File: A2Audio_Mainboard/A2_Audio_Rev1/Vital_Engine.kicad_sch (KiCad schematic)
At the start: 13 parts, among them J4 Micro_SD_Card, J5 Conn_01x15, U26 TS5A3159DBVR

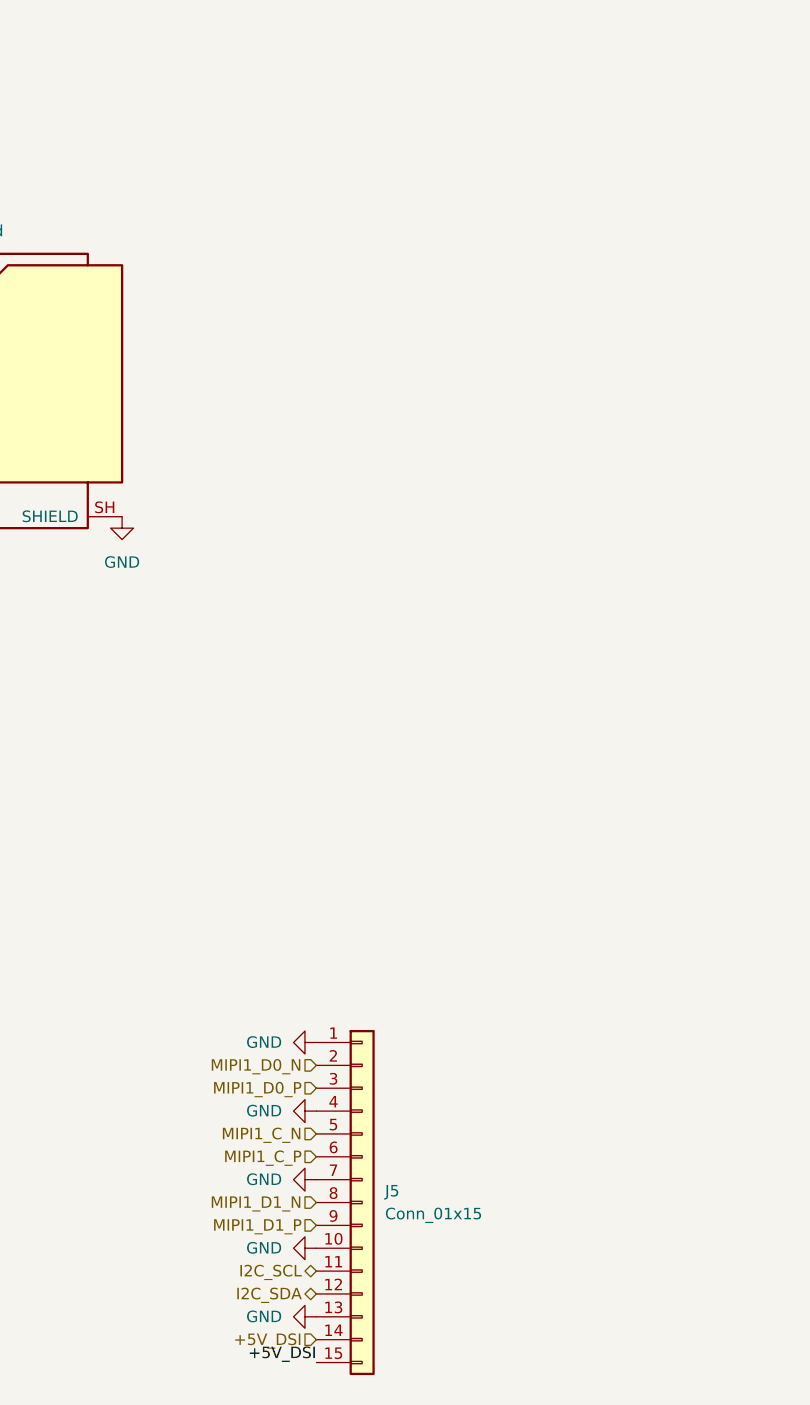
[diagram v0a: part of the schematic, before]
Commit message: Added footprints and a few more parts.
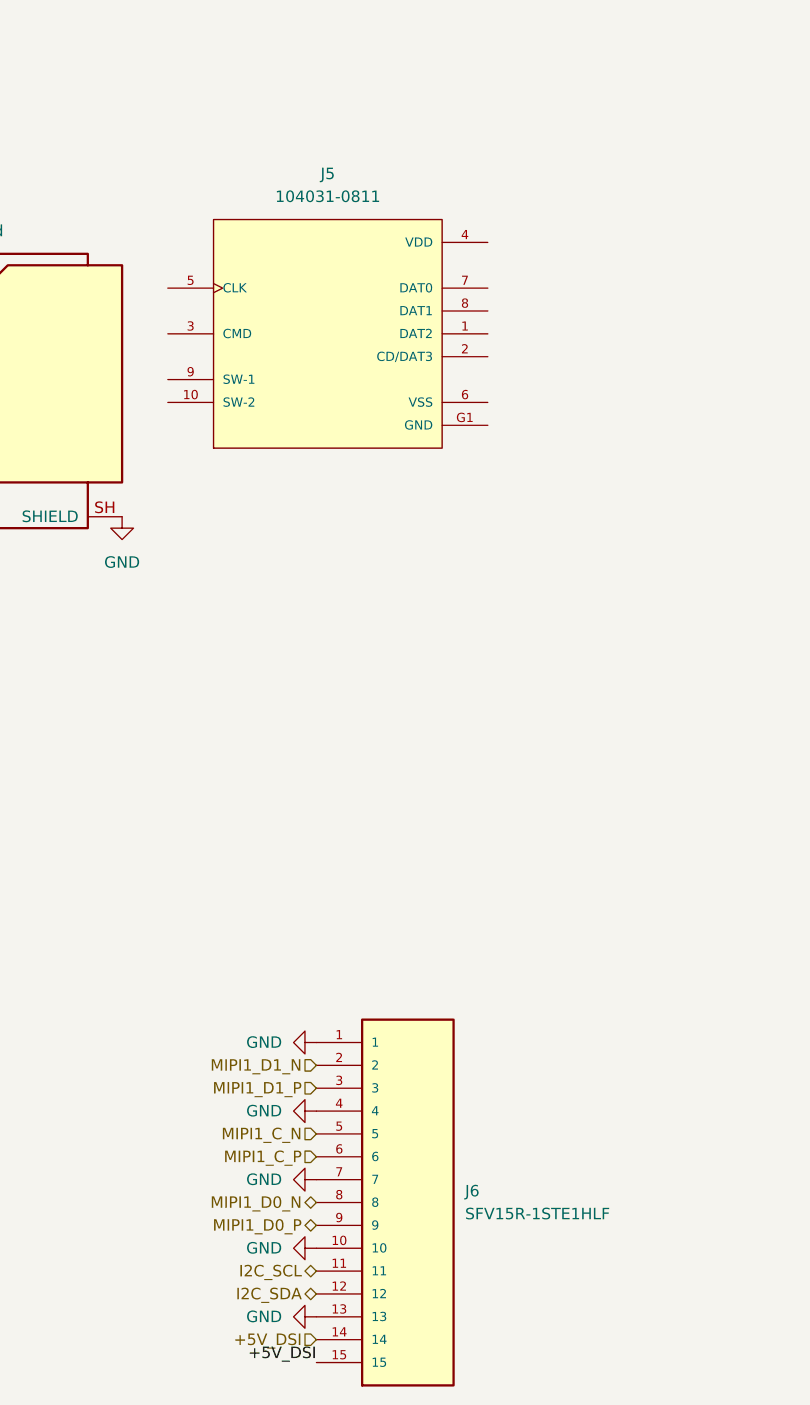
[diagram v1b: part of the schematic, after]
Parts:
- removed J5: Conn_01x15, symbol symbols:Conn_01x15
- added J5: 104031-0811, 104031-0811:MOLEX_104031-0811, symbol 104031-0811:104031-0811
- added J6: SFV15R-1STE1HLF, custom:AMPHENOL_SFV15R-1STE1HLF, symbol SFV15R-1STE1HLF:SFV15R-1STE1HLF
- C91, C93, C94: footprint (none) -> Capacitor_SMD:C_0402_1005Metric
- FB1: footprint (none) -> Inductor_SMD:L_0805_2012Metric
- R10, R37, R38, R39, R40, R7: footprint (none) -> Resistor_SMD:R_0402_1005Metric
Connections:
- net +5V_DSI: now also J6.14, J6.15
- net GND: now also J5.G1 (GND), J5.G2 (GND), J5.G3 (GND), J5.G4 (GND), J6.1, J6.10, J6.13, J6.4, J6.7
- net I2C_SCL: now also J6.11
- net I2C_SDA: now also J6.12
- net MIPI1_C_N: now also J6.5
- net MIPI1_C_P: now also J6.6
- net MIPI1_D0_N: now also J6.8
- net MIPI1_D0_P: now also J6.9
- net MIPI1_D1_N: now also J6.2
- net MIPI1_D1_P: now also J6.3

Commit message: More Refinement
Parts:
- removed J4: Micro_SD_Card, symbol symbols:Micro_SD_Card
- J5: footprint 104031-0811:MOLEX_104031-0811 -> Connector_Card:microSD_HC_Molex_104031-0811
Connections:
- net +3V3_SYS: now also J5.4 (VDD)
- net GND: now also J5.6 (VSS), J5.9 (SW-1)
- net SD_CLK: now also J5.5 (CLK)
- net SD_CMD: now also J5.3 (CMD)
- net SD_DAT0: now also J5.7 (DAT0)
- net SD_DAT1: now also J5.8 (DAT1)
- net SD_DAT2: now also J5.1 (DAT2)
- net SD_DAT3: now also J5.2 (CD/DAT3)

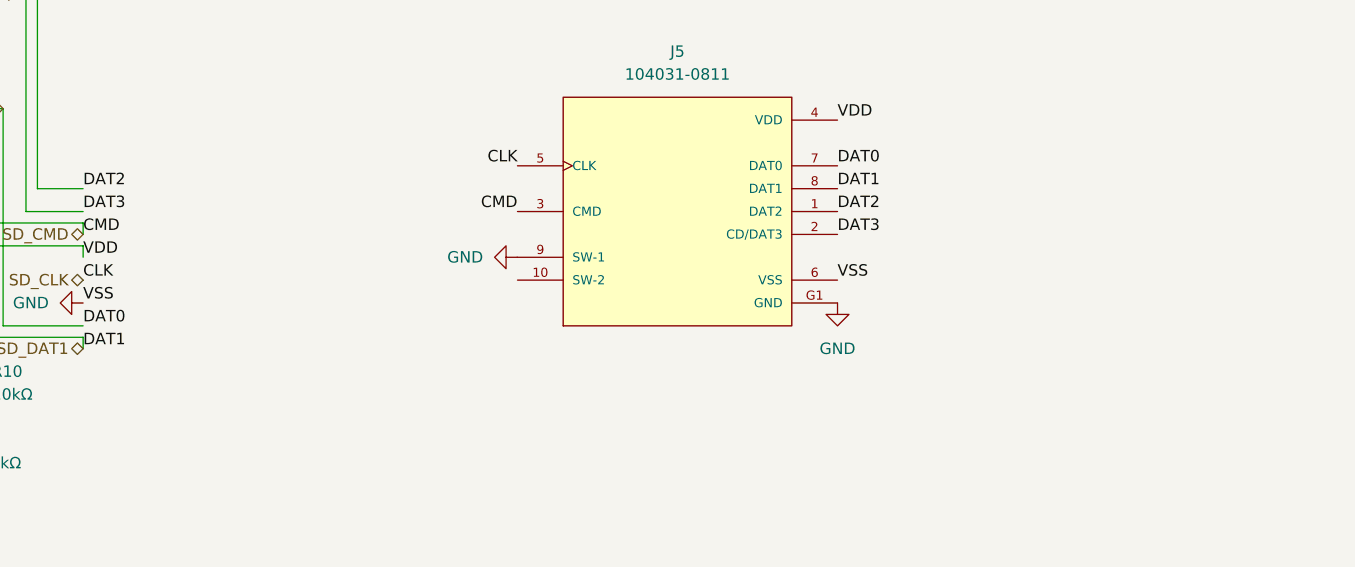
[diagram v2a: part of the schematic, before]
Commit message: Refining of logic and adding battery connector
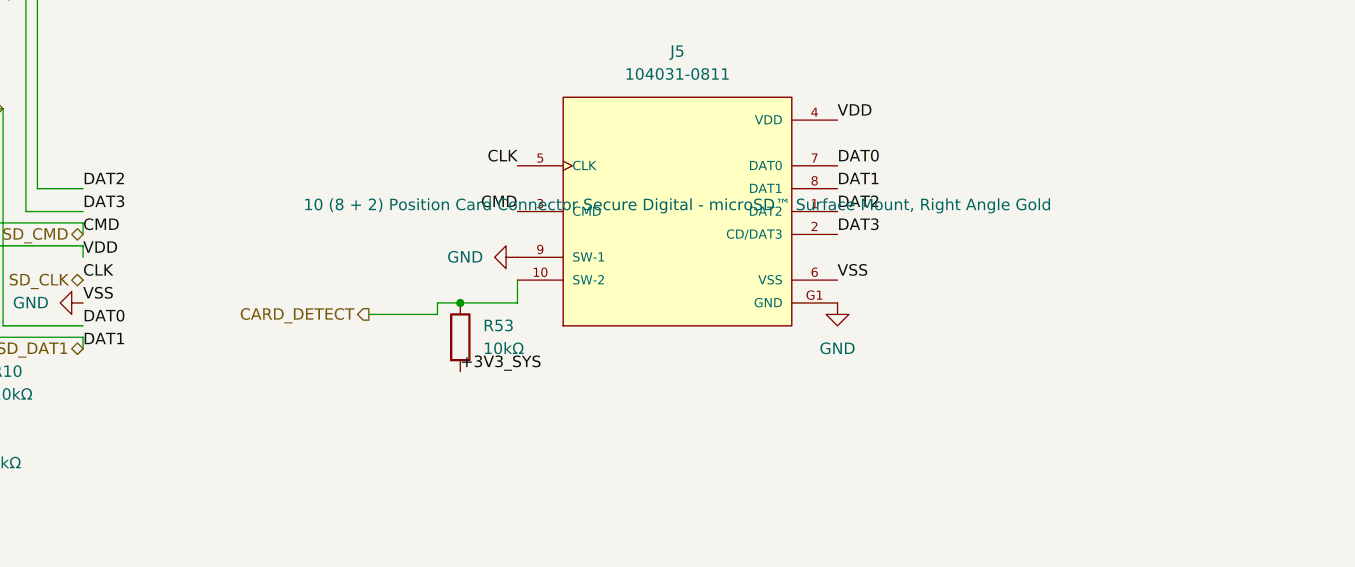
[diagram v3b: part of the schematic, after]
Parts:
- added R53: 10kΩ, Resistor_SMD:R_0402_1005Metric, symbol Device:R
- J5: footprint Connector_Card:microSD_HC_Molex_104031-0811 -> custom:MOLEX_104031-0811
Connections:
- net +3V3_SYS: now also R53.2
- net CARD_DETECT: now reaches J5.10 (SW-2)
- net CARD_DETECT: now also R53.1
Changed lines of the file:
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@@
 		(color 0 0 0 0)
 	)
+	(junction
+		(at 153.67 109.22)
+		(diameter 0)
+		(color 0 0 0 0)
+	)
 	(wire
 		(pts
@@
 	(wire
 		(pts
+			(xy 153.67 109.22) (xy 160.02 109.22)
+		)
+		(stroke
+			(width 0)
+			(type default)
+		)
+	)
+	(wire
+		(pts
 			(xy 97.79 100.33) (xy 97.79 121.92)
 		)
@@
 	(wire
 		(pts
+			(xy 151.13 110.49) (xy 151.13 109.22)
+		)
+		(stroke
+			(width 0)
+			(type default)
+		)
+	)
+	(wire
+		(pts
 			(xy 111.76 102.87) (xy 111.76 104.14)
 		)
@@
 	(wire
 		(pts
+			(xy 160.02 109.22) (xy 160.02 106.68)
+		)
+		(stroke
+			(width 0)
+			(type default)
+		)
+	)
+	(wire
+		(pts
 			(xy 111.76 113.03) (xy 99.06 113.03)
 		)
@@
 	(wire
 		(pts
+			(xy 151.13 109.22) (xy 153.67 109.22)
+		)
+		(stroke
+			(width 0)
+			(type default)
+		)
+	)
+	(wire
+		(pts
+			(xy 143.51 110.49) (xy 151.13 110.49)
+		)
+		(stroke
+			(width 0)
+			(type default)
+		)
+	)
+	(wire
+		(pts
 			(xy 106.68 96.52) (xy 111.76 96.52)
 		)
@@
 		)
 	)
+	(label "+3V3_SYS"
+		(at 153.67 116.84 0)
+		(effects
+			(font
+				(size 1.27 1.27)
+			)
+			(justify left bottom)
+		)
+	)
 	(label "DAT2"
 		(at 111.76 96.52 0)
@@
 		)
 	)
+	(hierarchical_label "CARD_DETECT"
+		(shape output)
+		(at 143.51 110.49 180)
+		(effects
+			(font
+				(size 1.27 1.27)
+			)
+			(justify right)
+		)
+	)
 	(hierarchical_label "SD_VDD_OVERRIDE"
 		(shape input)
@@
 	)
 	(symbol
+		(lib_id "Device:R")
+		(at 153.67 113.03 0)
+		(unit 1)
+		(body_style 1)
+		(exclude_from_sim no)
+		(in_bom yes)
+		(on_board yes)
+		(in_pos_files yes)
+		(dnp no)
+		(fields_autoplaced yes)
+		(property "Reference" "R53"
+			(at 156.21 111.7599 0)
+			(show_name no)
+			(do_not_autoplace no)
+			(effects
+				(font
+					(size 1.27 1.27)
+				)
+				(justify left)
+			)
+		)
+		(property "Value" "10kΩ"
+			(at 156.21 114.2999 0)
+			(show_name no)
+			(do_not_autoplace no)
+			(effects
+				(font
+					(size 1.27 1.27)
+				)
+				(justify left)
+			)
+		)
+		(property "Footprint" "Resistor_SMD:R_0402_1005Metric"
+			(at 151.892 113.03 90)
+			(hide yes)
+			(show_name no)
+			(do_not_autoplace no)
+			(effects
+				(font
+					(size 1.27 1.27)
+				)
+			)
+		)
+		(property "Datasheet" ""
+			(at 153.67 113.03 0)
+			(hide yes)
+			(show_name no)
+			(do_not_autoplace no)
+			(effects
+				(font
+					(size 1.27 1.27)
+				)
+			)
+		)
+		(property "Description" "Resistor"
+			(at 153.67 113.03 0)
+			(hide yes)
+			(show_name no)
+			(do_not_autoplace no)
+			(effects
+				(font
+					(size 1.27 1.27)
+				)
+			)
+		)
+		(pin "1"
+		)
+		(pin "2"
+		)
+		(instances
+			(project "A2_Audio_Rev1"
+				(path "/6bc02254-56bf-4f9a-8c1a-77c700c92092/76cb8377-ff36-43b7-a51c-57d5f70e1e39"
+					(reference "R53")
+					(unit 1)
+				)
+			)
+		)
+	)
+	(symbol
 		(lib_id "symbols:C")
 		(at 78.74 100.33 0)
@@
 			)
 		)
-		(property "Footprint" "Connector_Card:microSD_HC_Molex_104031-0811"
+		(property "Footprint" "custom:MOLEX_104031-0811"
 			(at 177.8 99.06 0)
 			(hide yes)
@@
 		(property "Description" "10 (8 + 2) Position Card Connector Secure Digital - microSD™ Surface Mount, Right Angle Gold"
 			(at 177.8 99.06 0)
-			(hide yes)
 			(show_name no)
 			(do_not_autoplace no)

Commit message: Final touches in schematic
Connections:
- net +5V_DSI is gone; now on net +3V3_SYS: J6.14, J6.15
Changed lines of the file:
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@@
 		)
 	)
-	(label "+5V_DSI"
+	(label "+3V3_SYS"
+		(at 176.53 210.82 180)
+		(effects
+			(font
+				(size 1.27 1.27)
+			)
+			(justify right bottom)
+		)
+	)
+	(label "+3V3_SYS"
 		(at 176.53 213.36 180)
 		(effects
@@
 		(effects
 			(font
-				(size 1.27 1.27)
-			)
-			(justify right)
-		)
-	)
-	(hierarchical_label "+5V_DSI"
-		(shape input)
-		(at 176.53 210.82 180)
-		(effects
-			(font

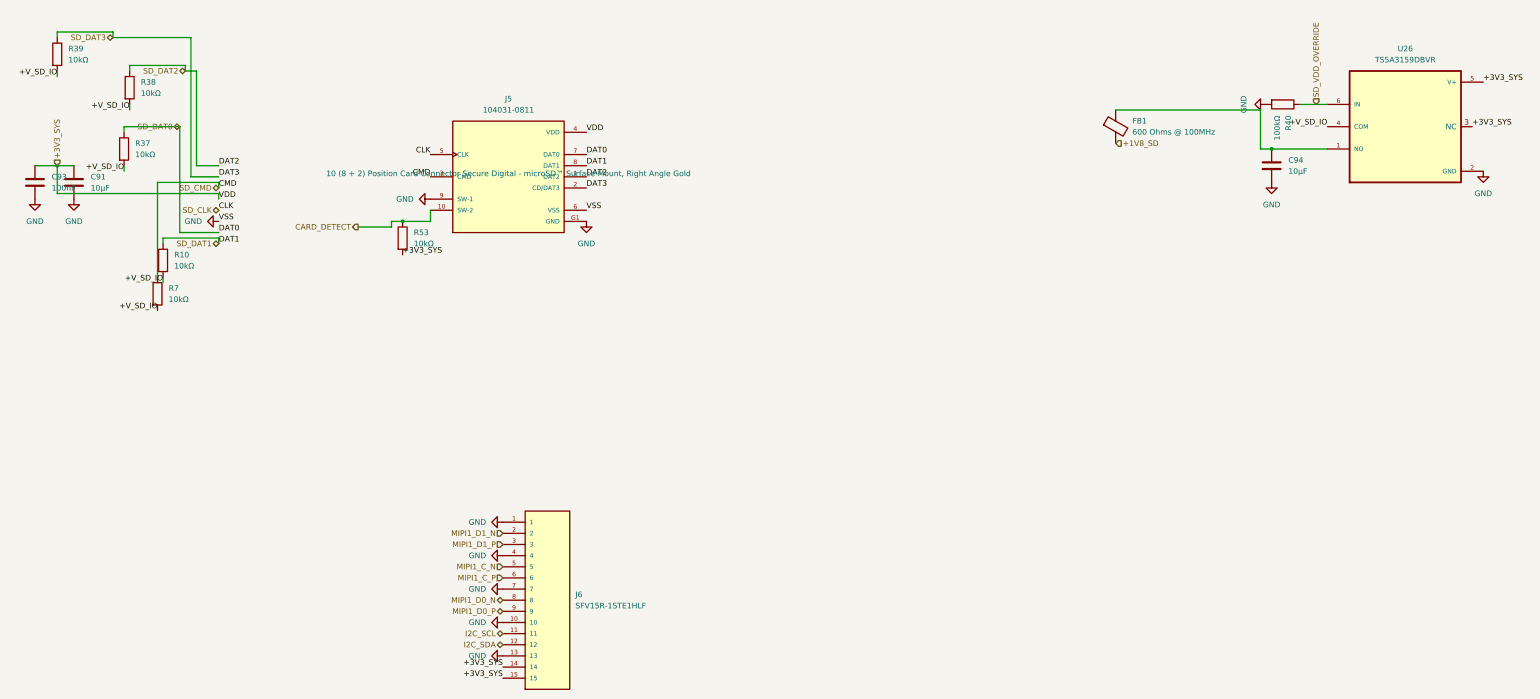
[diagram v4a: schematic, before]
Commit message: Fixed SD Card logic and power error
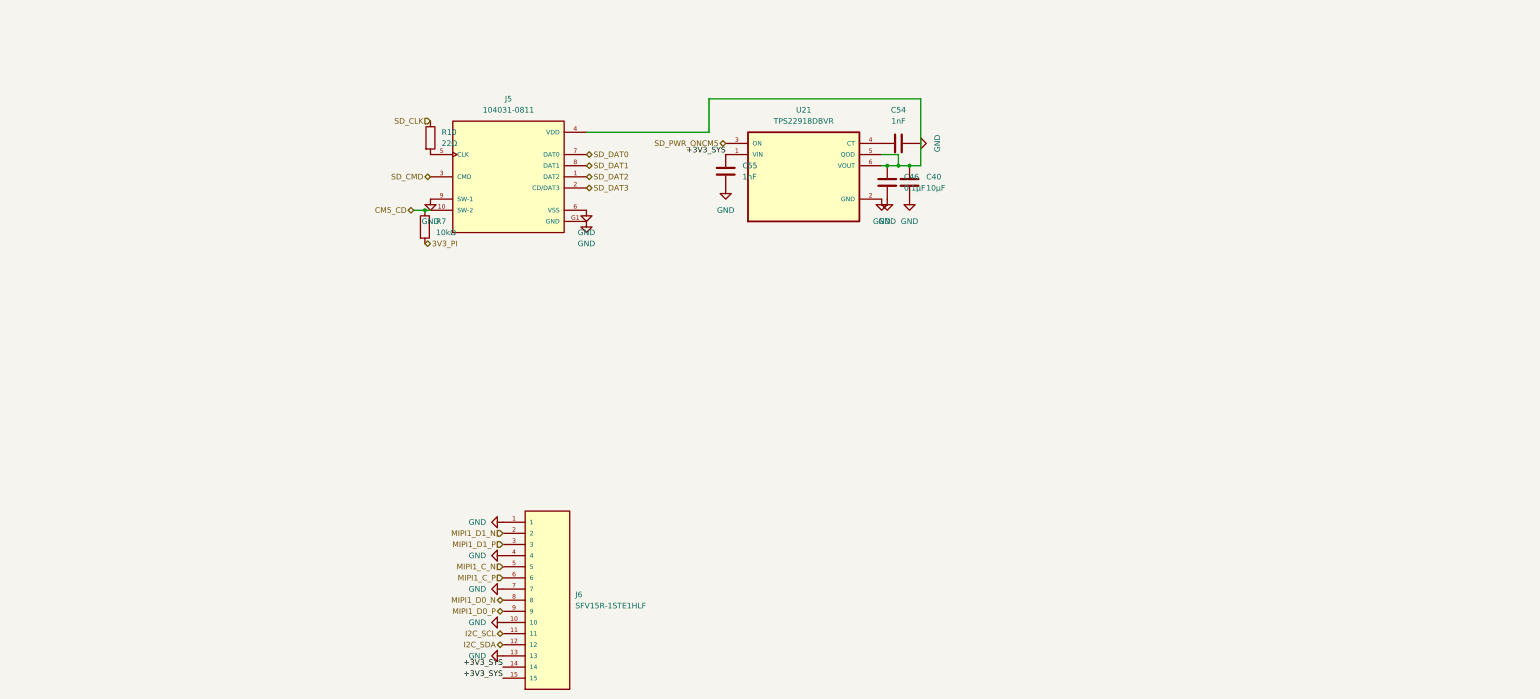
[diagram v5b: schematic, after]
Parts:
- removed C91, C94: 10µF, Capacitor_SMD:C_0402_1005Metric, symbol symbols:C
- removed C93: 100nF, Capacitor_SMD:C_0402_1005Metric, symbol symbols:C
- removed FB1: 600 Ohms @ 100MHz, Inductor_SMD:L_0805_2012Metric, symbol symbols:FerriteBead
- removed R37, R38, R39: 10kΩ, Resistor_SMD:R_0402_1005Metric, symbol symbols:R
- removed R40: 100kΩ, Resistor_SMD:R_0402_1005Metric, symbol symbols:R
- removed R53: 10kΩ, Resistor_SMD:R_0402_1005Metric, symbol Device:R
- removed U26: TS5A3159DBVR, custom:SOT95P280X145-6N, symbol TS5A3159DBVR:TS5A3159DBVR
- added C40: 10µF, symbol symbols:C
- added C46: 0.1µF, symbol symbols:C
- added C54, C55: 1nF, symbol symbols:C
- added U21: TPS22918DBVR, TPS22918DBVR:SOT95P280X145-6N, symbol TPS22918DBVR:TPS22918DBVR
- R10: value 10kΩ -> 22Ω; footprint Resistor_SMD:R_0402_1005Metric -> (none)
- R7: footprint Resistor_SMD:R_0402_1005Metric -> (none)
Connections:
- net +3V3_SYS: now also C55.2, U21.1 (VIN); no longer J5.4 (VDD)
- net GND: now also C40.2, C46.2, C54.2, C55.1, U21.2 (GND)
- net SD_CLK: now also R10.1; no longer J5.5 (CLK)
- net SD_CMD: no longer R7.1
- net SD_DAT1: no longer R10.1
- net +V_SD_IO: no longer names the net of R10.2
- net +V_SD_IO: now also J5.5 (CLK); no longer R7.2
- net CARD_DETECT renamed CM5_CD
- net CM5_CD: now also R7.1
- new net: C40.1, C46.1, J5.4 (VDD), U21.5 (QOD), U21.6 (VOUT)
- new net: C54.1, U21.4 (CT)
- new net 3V3_PI: R7.2
- new net SD_PWR_ONCM5: U21.3 (ON)
